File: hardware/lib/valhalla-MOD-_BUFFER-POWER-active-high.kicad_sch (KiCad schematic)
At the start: 1 part, among them U2 74LS06

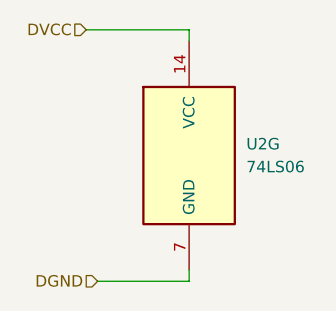
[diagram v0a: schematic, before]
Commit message: ADD: Valhalla-MOD XVR(RS485)
  - started work on the UART to RS-485 transceiver module, got stuck on
    finding a part that can either work on both 5 and 3.3V OR that has
    5V-tolerant inputs.
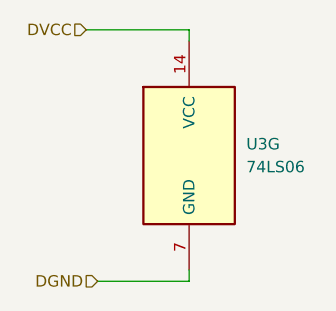
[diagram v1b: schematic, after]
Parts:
- renumbered U2 to U3
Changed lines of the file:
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@@
 		(dnp no)
 		(fields_autoplaced yes)
-		(property "Reference" "U2"
+		(property "Reference" "U3"
 			(at 133.35 82.5499 0)
 			(effects
@@
 		(instances
 			(project "valhalla-MOD-CPU_ATMEGA"
-				(path "/f06f94c1-3b85-417f-a10f-1ec163aec97d/f41873cd-99fe-4109-b415-d5d53cf2cc33"
-					(reference "U2")
+				(path "/f06f94c1-3b85-417f-a10f-1ec163aec97d/0e56eb88-dab4-4900-aca0-5fdf3b4369a1"
+					(reference "U3")
 					(unit 7)
 				)
